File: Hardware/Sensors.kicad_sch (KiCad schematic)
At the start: 0 parts

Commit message: Sensor completed
Barometer circuit done.
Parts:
- added C12, C18: 100nF, symbol Device:C
- added R19, R20: 10K, symbol Device:R
- added U6: DPS310, XDCR_DPS310, symbol iclr:DPS310
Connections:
- new net +3V3: C12.1, C18.2, R19.1, R20.1, U6.6 (VDDIO), U6.8 (VDD)
- new net GND: C12.2, C18.1, U6.1 (GND), U6.7 (GND)
- new net SCK: R20.2, U6.4 (SCK)
- new net SDI: R19.2, U6.3 (SDI)

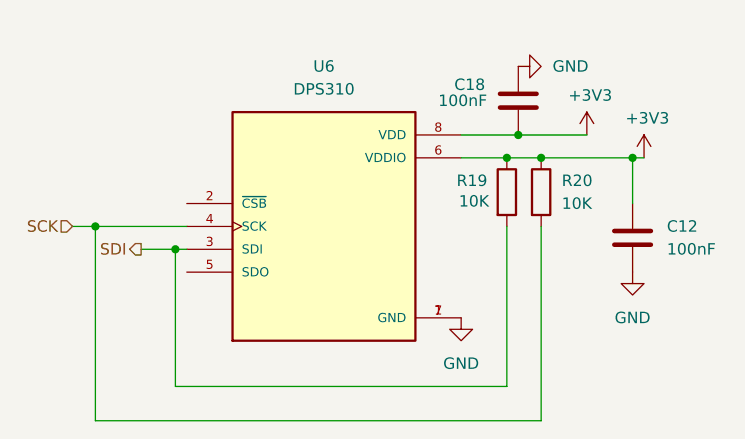
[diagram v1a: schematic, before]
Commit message: Barometer sensor SPI
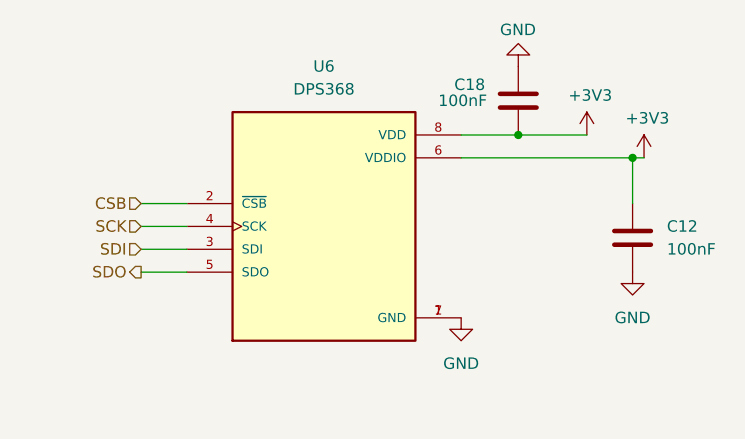
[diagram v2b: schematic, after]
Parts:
- removed R19, R20: 10K, symbol Device:R
- U6: value DPS310 -> DPS368
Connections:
- net CSB: now reaches U6.2 (~{CSB})
- net SDO: now reaches U6.5 (SDO)

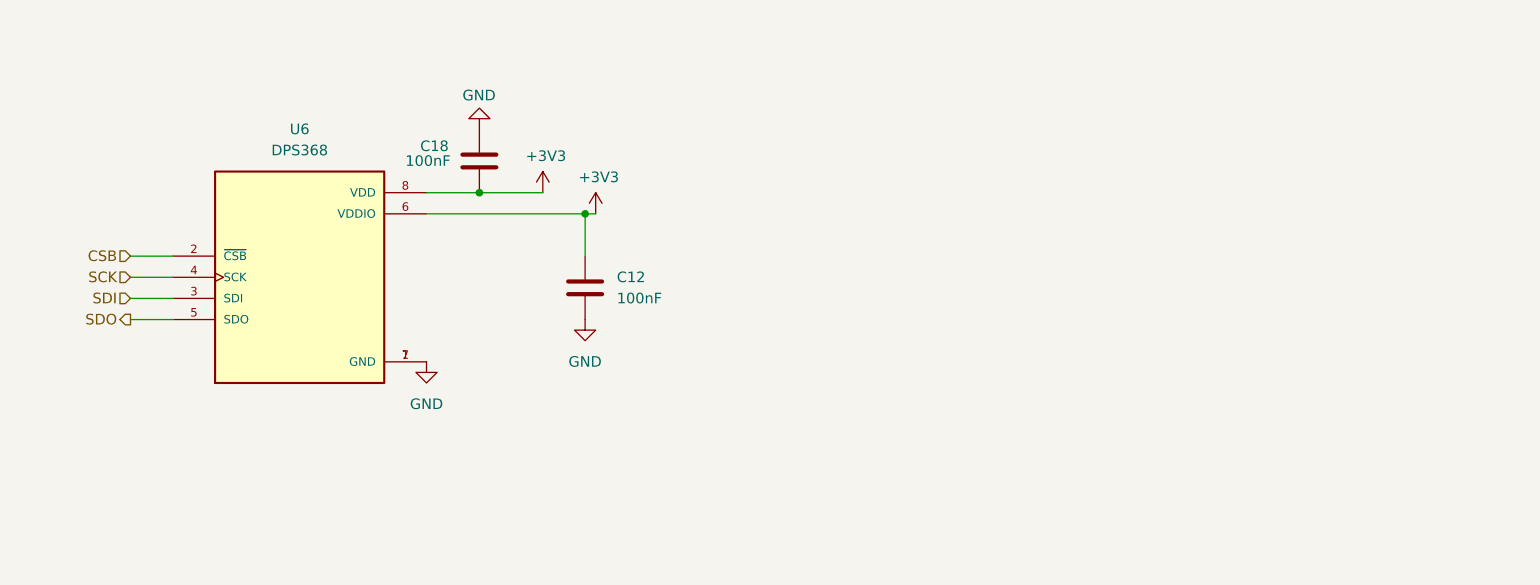
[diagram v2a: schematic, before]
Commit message: Barometer fix + Photo sensor
Fixed orientation of ground for barometer. Added Photo sensor + photo sensor symbol in library.

Need to determine resistance for photo sensor circuit.
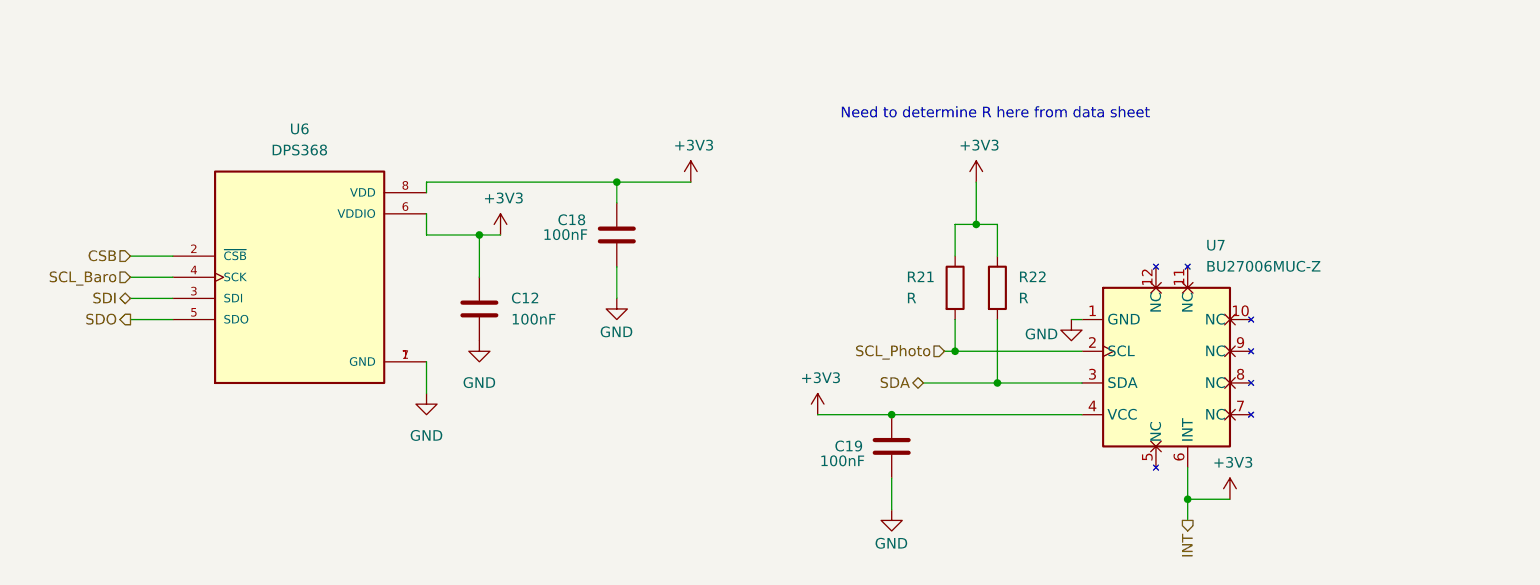
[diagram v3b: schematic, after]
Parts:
- added C19: 100nF, symbol Device:C
- added R21, R22: R, symbol Device:R
- added U7: BU27006MUC-Z, symbol Recovery-line-cutter-library:BU27006MUC-Z
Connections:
- net +3V3: now also C18.1, C19.1, R21.1, R22.1, U7.4 (VCC), U7.6 (INT); no longer C18.2
- net GND: now also C18.2, C19.2, U7.1 (GND); no longer C18.1
- net SCK renamed SCL_Baro
- new net SCL_Photo: R21.2, U7.2 (SCL)
- new net SDA: R22.2, U7.3 (SDA)
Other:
- note added: "Need to determine R here from data sheet"
- moved on the sheet: C12, C18

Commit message: USB-C + Voltage stuff
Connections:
- net SDA renamed SDA_Photo
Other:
- note added: "Need to determine R here from data sheet High resistance to keep pins high Find library for BU27006MUC-Z + use that symbol (should be on mouser)"
- note removed: "Need to determine R here from data sheet"
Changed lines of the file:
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@@
 		)
 	)
-	(text "Need to determine R here from data sheet"
+	(text "Need to determine R here from data sheet\n\nHigh resistance to keep pins high\n\nFind library for BU27006MUC-Z + use that symbol (should be on mouser)"
 		(exclude_from_sim no)
-		(at 223.266 60.452 0)
+		(at 243.586 54.356 0)
 		(effects
 			(font
@@
 		)
 	)
-	(hierarchical_label "SDA"
+	(hierarchical_label "SDA_Photo"
 		(shape bidirectional)
 		(at 214.63 92.71 180)

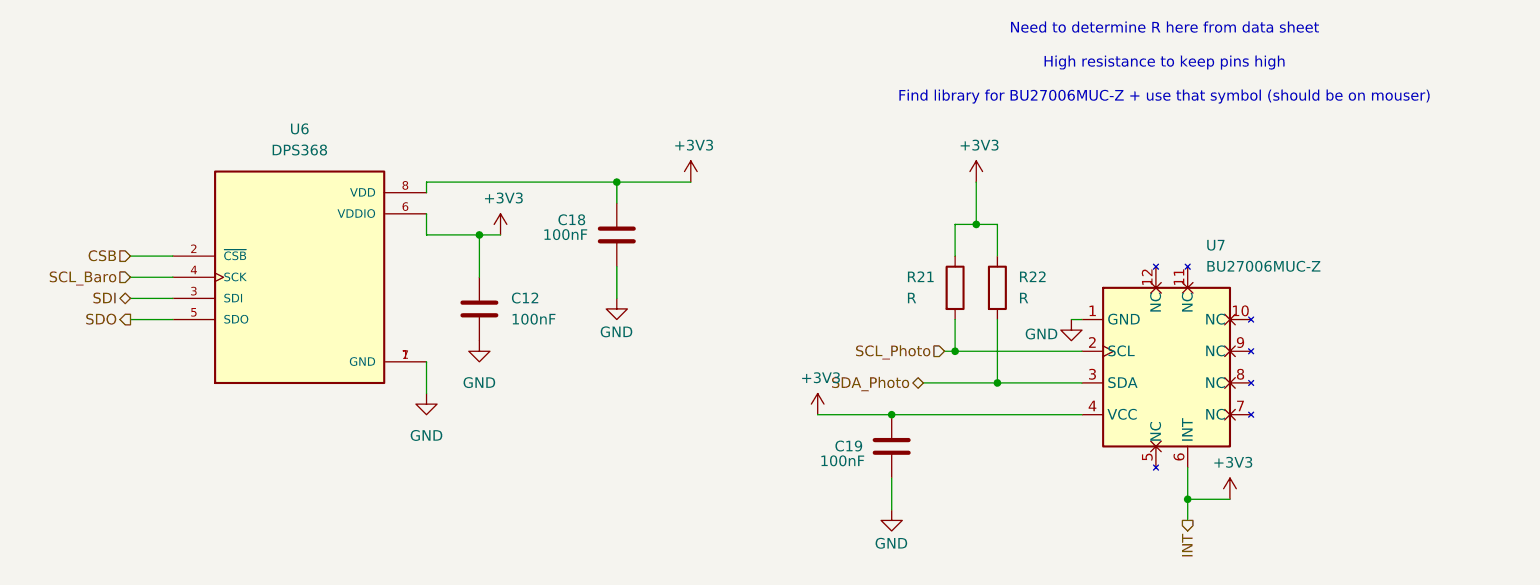
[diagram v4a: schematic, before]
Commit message: Voltage regulation done + used photo ic sensor library
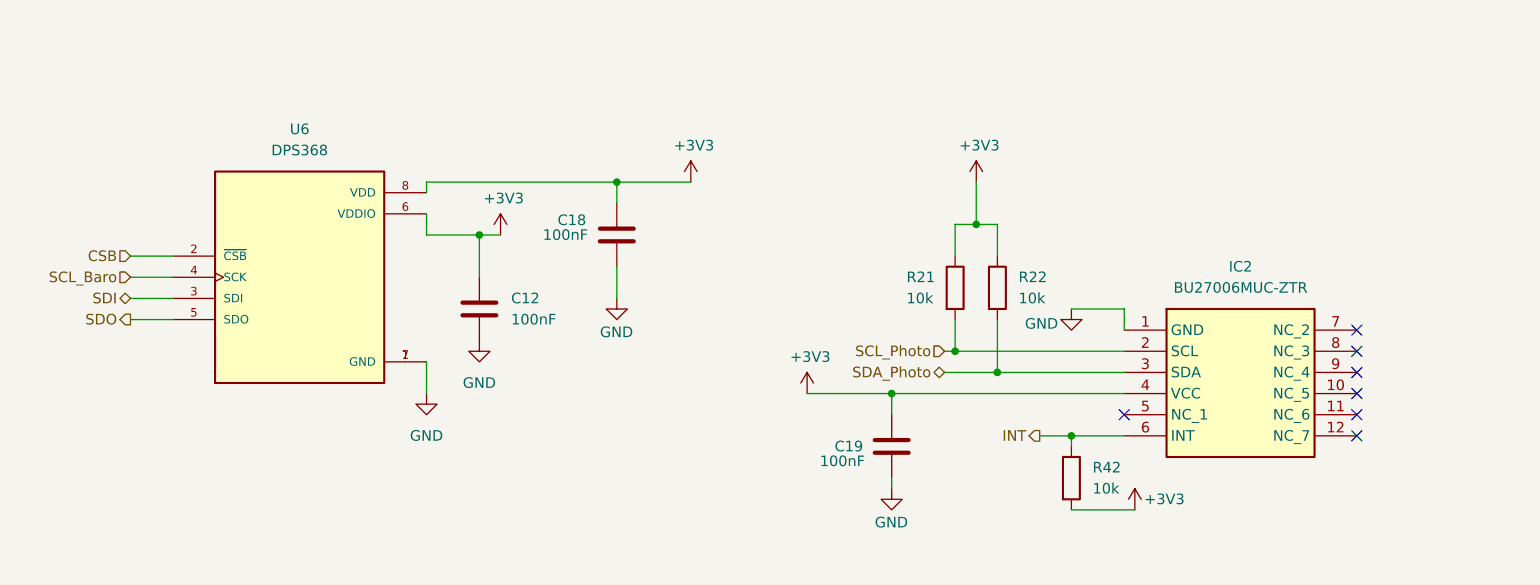
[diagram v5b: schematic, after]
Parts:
- removed U7: BU27006MUC-Z, symbol Recovery-line-cutter-library:BU27006MUC-Z
- added IC2: BU27006MUC-ZTR, BU27006MUCZTR, symbol iclr:BU27006MUC-ZTR
- added R42: 10k, symbol Device:R
- R21, R22: value R -> 10k
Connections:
- net +3V3: now also IC2.4 (VCC), R42.2
- net GND: now also IC2.1 (GND)
- net SCL_Photo: now also IC2.2 (SCL)
- net SDA_Photo: now also IC2.3 (SDA)
- new net INT: IC2.6 (INT), R42.1
- no-connect marks 0 -> 7
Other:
- note removed: "Need to determine R here from data sheet High resistance to keep pins high Find library for BU27006MUC-Z + use that symbol (should be on mouser)"

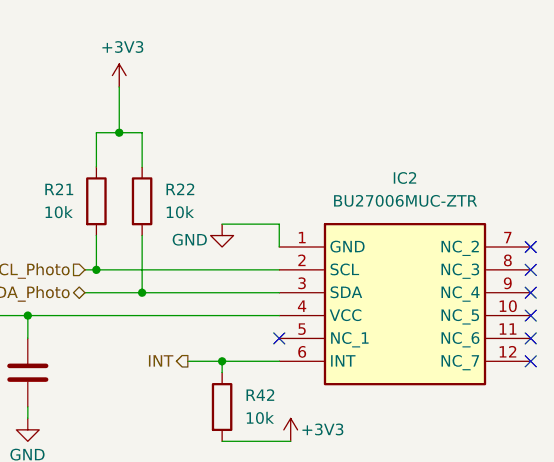
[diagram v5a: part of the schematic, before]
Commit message: New Buck boost converter
+ new sorted circuit, voltage regulation not finalised
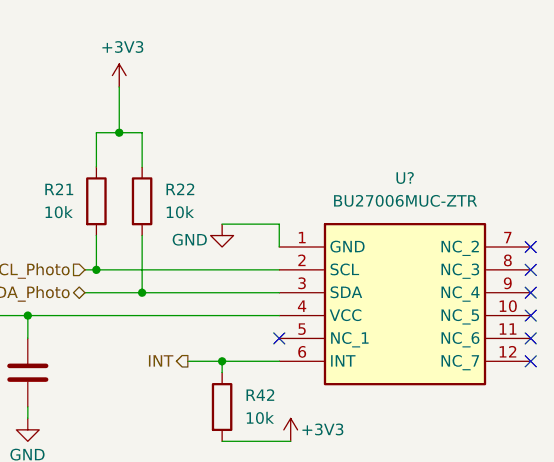
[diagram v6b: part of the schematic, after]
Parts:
- renumbered IC2 to U?
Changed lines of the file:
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@@
 		(dnp no)
 		(fields_autoplaced yes)
-		(property "Reference" "IC2"
+		(property "Reference" "U?"
 			(at 252.73 78.74 0)
 			(effects
@@
 			(project ""
 				(path "/7db990e4-92e1-4f99-b4d2-435bbec1ba83/d9e876a4-516f-4c0a-b39c-c20b5b59833a"
-					(reference "IC2")
+					(reference "U?")
 					(unit 1)
 				)

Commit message: PCB mid design
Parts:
- removed U6: DPS368, XDCR_DPS310, symbol iclr:DPS310
- added U11: DPS368, iclr:XDCR_DPS310, symbol iclr:DPS310
- C12, C18, C19: footprint (none) -> Capacitor_SMD:C_0402_1005Metric
- R21, R22, R42: footprint (none) -> Resistor_SMD:R_0402_1005Metric
- U7: renamed from U?; footprint BU27006MUCZTR -> iclr:BU27006MUCZTR
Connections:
- net +3V3: now also U11.6 (VDDIO), U11.8 (VDD)
- net CSB: now also U11.2 (~{CSB})
- net GND: now also U11.1 (GND), U11.7 (GND)
- net SCL_Baro: now also U11.4 (SCK)
- net SDI: now also U11.3 (SDI)
- net SDO: now also U11.5 (SDO)
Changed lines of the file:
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@@
 			)
 		)
-		(property "Footprint" ""
+		(property "Footprint" "Resistor_SMD:R_0402_1005Metric"
 			(at 221.742 81.28 90)
 			(effects
@@
 		(on_board yes)
 		(dnp no)
-		(property "Reference" "#PWR028"
+		(property "Reference" "#PWR0101"
 			(at 186.69 72.39 0)
 			(effects
@@
 			(project "Main board"
 				(path "/7db990e4-92e1-4f99-b4d2-435bbec1ba83/d9e876a4-516f-4c0a-b39c-c20b5b59833a"
-					(reference "#PWR028")
+					(reference "#PWR0101")
 					(unit 1)
 				)
@@
 			)
 		)
-		(property "Footprint" ""
+		(property "Footprint" "Capacitor_SMD:C_0402_1005Metric"
 			(at 162.2552 87.63 0)
 			(effects
@@
 		(on_board yes)
 		(dnp no)
-		(property "Reference" "#PWR046"
+		(property "Reference" "#PWR0103"
 			(at 163.83 78.74 0)
 			(effects
@@
 			(project "Main board"
 				(path "/7db990e4-92e1-4f99-b4d2-435bbec1ba83/d9e876a4-516f-4c0a-b39c-c20b5b59833a"
-					(reference "#PWR046")
+					(reference "#PWR0103")
 					(unit 1)
 				)
@@
 		(dnp no)
 		(fields_autoplaced yes)
-		(property "Reference" "#PWR016"
+		(property "Reference" "#PWR0104"
 			(at 154.94 100.33 0)
 			(effects
@@
 			(project ""
 				(path "/7db990e4-92e1-4f99-b4d2-435bbec1ba83/d9e876a4-516f-4c0a-b39c-c20b5b59833a"
-					(reference "#PWR016")
+					(reference "#PWR0104")
 					(unit 1)
 				)
@@
 		(dnp no)
 		(fields_autoplaced yes)
-		(property "Reference" "U?"
+		(property "Reference" "U7"
 			(at 252.73 78.74 0)
 			(effects
@@
 			)
 		)
-		(property "Footprint" "BU27006MUCZTR"
+		(property "Footprint" "iclr:BU27006MUCZTR"
 			(at 262.89 181.28 0)
 			(effects
@@
 			(project ""
 				(path "/7db990e4-92e1-4f99-b4d2-435bbec1ba83/d9e876a4-516f-4c0a-b39c-c20b5b59833a"
-					(reference "U?")
+					(reference "U7")
+					(unit 1)
+				)
+			)
+		)
+	)
+	(symbol
+		(lib_id "iclr:DPS310")
+		(at 139.7 80.01 0)
+		(unit 1)
+		(exclude_from_sim no)
+		(in_bom yes)
+		(on_board yes)
+		(dnp no)
+		(fields_autoplaced yes)
+		(property "Reference" "U11"
+			(at 139.7 62.23 0)
+			(effects
+				(font
+					(size 1.27 1.27)
+				)
+			)
+		)
+		(property "Value" "DPS368"
+			(at 139.7 64.77 0)
+			(effects
+				(font
+					(size 1.27 1.27)
+				)
+			)
+		)
+		(property "Footprint" "iclr:XDCR_DPS310"
+			(at 139.7 80.01 0)
+			(effects
+				(font
+					(size 1.27 1.27)
+				)
+				(justify bottom)
+				(hide yes)
+			)
+		)
+		(property "Datasheet" "https://www.infineon.com/dgdl/Infineon-DPS368-DataSheet-v01_01-EN.pdf?fileId=5546d46269e1c019016a0c45105d4b40"
+			(at 139.7 80.01 0)
+			(effects
+				(font
+					(size 1.27 1.27)
+				)
+				(hide yes)
+			)
+		)
+		(property "Description" "Supply voltage range 1.7V to 3.6V | Operation range 300hPa 1200hPa | Sensors precision 0.005hPa | Relative accuracy 0.06hPa | Pressure temperature sensitivity of 0.5Pa/K | Temperature accuracy 0.5C"
+			(at 139.7 80.01 0)
+			(effects
+				(font
+					(size 1.27 1.27)
+				)
+				(justify bottom)
+				(hide yes)
+			)
+		)
+		(property "AVAILABILITY" "Unavailable"
+			(at 139.7 80.01 0)
+			(effects
+				(font
+					(size 1.27 1.27)
+				)
+				(justify bottom)
+				(hide yes)
+			)
+		)
+		(property "MP" "DPS310XTSA1"
+			(at 139.7 80.01 0)
+			(effects
+				(font
+					(size 1.27 1.27)
+				)
+				(justify bottom)
+				(hide yes)
+			)
+		)
+		(property "PRICE" "None"
+			(at 139.7 80.01 0)
+			(effects
+				(font
+					(size 1.27 1.27)
+				)
+				(justify bottom)
+				(hide yes)
+			)
+		)
+		(property "PACKAGE" "LGA-8 Infineon"
+			(at 139.7 80.01 0)
+			(effects
+				(font
+					(size 1.27 1.27)
+				)
+				(justify bottom)
+				(hide yes)
+			)
+		)
+		(property "MF" "Infineon"
+			(at 139.7 80.01 0)
+			(effects
+				(font
+					(size 1.27 1.27)
+				)
+				(justify bottom)
+				(hide yes)
+			)
+		)
+		(pin "6"
+		)
+		(pin "2"
+		)
+		(pin "4"
+		)
+		(pin "1"
+		)
+		(pin "5"
+		)
+		(pin "3"
+		)
+		(pin "8"
+		)
+		(pin "7"
+		)
+		(instances
+			(project ""
+				(path "/7db990e4-92e1-4f99-b4d2-435bbec1ba83/d9e876a4-516f-4c0a-b39c-c20b5b59833a"
+					(reference "U11")
 					(unit 1)
 				)
@@
 			)
 		)
-		(property "Footprint" ""
+		(property "Footprint" "Resistor_SMD:R_0402_1005Metric"
 			(at 230.632 104.14 90)
 			(effects
@@
 			)
 		)
-		(property "Footprint" ""
+		(property "Footprint" "Capacitor_SMD:C_0402_1005Metric"
 			(at 211.7852 104.14 0)
 			(effects
@@
 			)
 		)
-		(property "Footprint" ""
+		(property "Footprint" "Resistor_SMD:R_0402_1005Metric"
 			(at 216.662 81.28 90)
 			(effects
@@
 	)
 	(symbol
-		(lib_id "iclr:DPS310")
-		(at 139.7 80.01 0)
-		(unit 1)
-		(exclude_from_sim no)
-		(in_bom yes)
-		(on_board yes)
-		(dnp no)
-		(fields_autoplaced yes)
-		(property "Reference" "U6"
-			(at 139.7 62.23 0)
-			(effects
-				(font
-					(size 1.27 1.27)
-				)
-			)
-		)
-		(property "Value" "DPS368"
-			(at 139.7 64.77 0)
-			(effects
-				(font
-					(size 1.27 1.27)
-				)
-			)
-		)
-		(property "Footprint" "XDCR_DPS310"
-			(at 139.7 80.01 0)
-			(effects
-				(font
-					(size 1.27 1.27)
-				)
-				(justify bottom)
-				(hide yes)
-			)
-		)
-		(property "Datasheet" ""
-			(at 139.7 80.01 0)
-			(effects
-				(font
-					(size 1.27 1.27)
-				)
-				(hide yes)
-			)
-		)
-		(property "Description" "Supply voltage range 1.7V to 3.6V | Operation range 300hPa 1200hPa | Sensors precision 0.005hPa | Relative accuracy 0.06hPa | Pressure temperature sensitivity of 0.5Pa/K | Temperature accuracy 0.5C"
-			(at 139.7 80.01 0)
-			(effects
-				(font
-					(size 1.27 1.27)
-				)
-				(justify bottom)
-				(hide yes)
-			)
-		)
-		(property "AVAILABILITY" "Unavailable"
-			(at 139.7 80.01 0)
-			(effects
-				(font
-					(size 1.27 1.27)
-				)
-				(justify bottom)
-				(hide yes)
-			)
-		)
-		(property "MP" "DPS310XTSA1"
-			(at 139.7 80.01 0)
-			(effects
-				(font
-					(size 1.27 1.27)
-				)
-				(justify bottom)
-				(hide yes)
-			)
-		)
-		(property "PRICE" "None"
-			(at 139.7 80.01 0)
-			(effects
-				(font
-					(size 1.27 1.27)
-				)
-				(justify bottom)
-				(hide yes)
-			)
-		)
-		(property "PACKAGE" "LGA-8 Infineon"
-			(at 139.7 80.01 0)
-			(effects
-				(font
-					(size 1.27 1.27)
-				)
-				(justify bottom)
-				(hide yes)
-			)
-		)
-		(property "MF" "Infineon"
-			(at 139.7 80.01 0)
-			(effects
-				(font
-					(size 1.27 1.27)
-				)
-				(justify bottom)
-				(hide yes)
-			)
-		)
-		(pin "1"
-		)
-		(pin "4"
-		)
-		(pin "2"
-		)
-		(pin "3"
-		)
-		(pin "6"
-		)
-		(pin "8"
-		)
-		(pin "5"
-		)
-		(pin "7"
-		)
-		(instances
-			(project ""
-				(path "/7db990e4-92e1-4f99-b4d2-435bbec1ba83/d9e876a4-516f-4c0a-b39c-c20b5b59833a"
-					(reference "U6")
-					(unit 1)
-				)
-			)
-		)
-	)
-	(symbol
 		(lib_id "power:+3.3V")
 		(at 240.03 107.95 0)
@@
 			)
 		)
-		(property "Footprint" ""
+		(property "Footprint" "Capacitor_SMD:C_0402_1005Metric"
 			(at 178.7652 78.74 0)
 			(effects
@@
 		(on_board yes)
 		(dnp no)
-		(property "Reference" "#PWR051"
+		(property "Reference" "#PWR0102"
 			(at 177.8 88.9 0)
 			(effects
@@
 			(project "Main board"
 				(path "/7db990e4-92e1-4f99-b4d2-435bbec1ba83/d9e876a4-516f-4c0a-b39c-c20b5b59833a"
-					(reference "#PWR051")
-					(unit 1)
-				)
+					(reference "#PWR0102")
+					(unit 1)
+				)
